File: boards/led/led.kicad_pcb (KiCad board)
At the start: 2 copper layers, 20 x 20 mm, 2 parts, among them J1 RJ45

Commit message: led pcb
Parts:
- moved J1 3.24 mm to (176.5, 104.1)
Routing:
- net Net-(D1-Pad2): track 0.00 -> 65.5 mm, vias 0 -> 1
- net Net-(D1-Pad1): track 0.00 -> 65.0 mm, vias 0 -> 1
- net Net-(D1-Pad3): track 0.00 -> 59.5 mm
- net Net-(D1-Pad4): track 0.00 -> 11.2 mm, vias 0 -> 1
- net Net-(D1-Pad5): track 0.00 -> 10.7 mm, vias 0 -> 1
- net Net-(D1-Pad6): track 0.00 -> 9.59 mm
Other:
- board size 20 x 20 mm -> 52.1 x 27.9 mm
- net class Default: clearance 0.4 -> 0.2; trace_width 0.25 -> 0.4
- rule trace_clearance: 0.4 -> 0.2
- board text added: "CUTOUT"
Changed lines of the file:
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@@
   (general
     (links 6)
-    (no_connects 6)
-    (area 0 0 0 0)
+    (no_connects 0)
+    (area 132.004999 90.094999 184.729001 118.185001)
     (thickness 1.6)
-    (drawings 4)
-    (tracks 0)
+    (drawings 9)
+    (tracks 38)
     (zones 0)
     (modules 2)
@@
   )
   (setup
-    (last_trace_width 0.25)
-    (trace_clearance 0.4)
+    (last_trace_width 0.4)
+    (trace_clearance 0.2)
     (zone_clearance 0.508)
     (zone_45_only yes)
@@
   (net 8 "Net-(J1-Pad8)")
   (net_class Default "This is the default net class."
-    (clearance 0.4)
-    (trace_width 0.25)
+    (clearance 0.2)
+    (trace_width 0.4)
     (via_dia 0.6)
     (via_drill 0.4)
@@
   )
   (module Connect:RJ45_8 (layer F.Cu)
-    (at 179.705 103.505 90)
+    (at 176.53 104.14 90)
     (tags RJ45)
     (fp_text reference J1 (at 0.254 4.826 90) (layer F.SilkS)
@@
     )
   )
+  (gr_line (start 132.08 118.11) (end 184.15 118.11) (angle 90) (layer Edge.Cuts) (width 0.15))
+  (gr_line (start 132.08 90.17) (end 132.08 118.11) (angle 90) (layer Edge.Cuts) (width 0.15))
+  (gr_line (start 184.15 90.17) (end 132.08 90.17) (angle 90) (layer Edge.Cuts) (width 0.15))
+  (gr_line (start 184.15 118.11) (end 184.15 90.17) (angle 90) (layer Edge.Cuts) (width 0.15))
+  (gr_text CUTOUT (at 149.225 104.775) (layer F.SilkS)
+    (effects (font (size 1.5 1.5) (thickness 0.3)))
+  )
   (gr_line (start 139 115) (end 139 95) (angle 90) (layer Edge.Cuts) (width 0.15))
   (gr_line (start 159 115) (end 139 115) (angle 90) (layer Edge.Cuts) (width 0.15))
   (gr_line (start 159 95) (end 159 115) (angle 90) (layer Edge.Cuts) (width 0.15))
   (gr_line (start 139 95) (end 159 95) (angle 90) (layer Edge.Cuts) (width 0.15))
+  (segment (start 170.18 106.045) (end 170.815 106.045) (width 0.25) (layer F.Cu) (net 1) (status 30))
+  (segment (start 170.815 106.045) (end 172.72 106.68) (width 0.4) (layer F.Cu) (net 1) (status 10))
+  (segment (start 172.72 106.68) (end 172.72 116.84) (width 0.4) (layer F.Cu) (net 1))
+  (segment (start 172.72 116.84) (end 134.62 116.84) (width 0.4) (layer F.Cu) (net 1))
+  (via (at 134.62 116.84) (size 0.6) (drill 0.4) (layers F.Cu B.Cu) (net 1))
+  (segment (start 134.62 116.84) (end 134.62 105.41) (width 0.4) (layer B.Cu) (net 1))
+  (segment (start 134.62 105.41) (end 135.03 105) (width 0.4) (layer B.Cu) (net 1))
+  (segment (start 135.03 105) (end 137.57 105) (width 0.4) (layer B.Cu) (net 1))
+  (segment (start 170.18 103.505) (end 170.815 103.505) (width 0.25) (layer B.Cu) (net 2) (status 30))
+  (segment (start 170.815 103.505) (end 172.72 104.14) (width 0.4) (layer B.Cu) (net 2) (status 10))
+  (segment (start 172.72 104.14) (end 172.72 116.84) (width 0.4) (layer B.Cu) (net 2))
+  (segment (start 172.72 116.84) (end 138.43 116.84) (width 0.4) (layer B.Cu) (net 2))
+  (segment (start 138.43 116.84) (end 137.57 116.43) (width 0.4) (layer B.Cu) (net 2))
+  (segment (start 137.57 116.43) (end 137.57 107.54) (width 0.4) (layer B.Cu) (net 2))
+  (segment (start 137.57 99.47) (end 137.57 102.46) (width 0.4) (layer B.Cu) (net 3))
+  (segment (start 137.16 99.06) (end 137.57 99.47) (width 0.4) (layer B.Cu) (net 3))
+  (via (at 137.16 99.06) (size 0.6) (drill 0.4) (layers F.Cu B.Cu) (net 3))
+  (segment (start 133.35 99.06) (end 137.16 99.06) (width 0.4) (layer F.Cu) (net 3))
+  (segment (start 133.35 102.87) (end 133.35 99.06) (width 0.4) (layer F.Cu) (net 3))
+  (segment (start 170.18 109.22) (end 166.37 115.57) (width 0.4) (layer F.Cu) (net 3) (status 10))
+  (segment (start 166.37 115.57) (end 133.35 115.57) (width 0.4) (layer F.Cu) (net 3))
+  (segment (start 133.35 115.57) (end 133.35 102.87) (width 0.4) (layer F.Cu) (net 3))
+  (segment (start 170.18 108.585) (end 170.18 109.22) (width 0.25) (layer F.Cu) (net 3) (status 30))
+  (segment (start 167.64 107.315) (end 167.64 106.68) (width 0.25) (layer B.Cu) (net 4) (status 10))
+  (segment (start 163.83 102.87) (end 160.84 102.87) (width 0.4) (layer B.Cu) (net 4))
+  (segment (start 167.64 106.68) (end 163.83 102.87) (width 0.4) (layer B.Cu) (net 4))
+  (segment (start 160.84 102.87) (end 160.43 102.46) (width 0.25) (layer B.Cu) (net 4))
+  (segment (start 167.64 104.775) (end 167.005 104.775) (width 0.25) (layer F.Cu) (net 5) (status 30))
+  (segment (start 167.005 104.775) (end 165.1 107.95) (width 0.4) (layer F.Cu) (net 5) (status 10))
+  (via (at 165.1 107.95) (size 0.6) (drill 0.4) (layers F.Cu B.Cu) (net 5))
+  (segment (start 165.1 107.95) (end 163.42 105) (width 0.4) (layer B.Cu) (net 5))
+  (segment (start 163.42 105) (end 160.43 105) (width 0.4) (layer B.Cu) (net 5))
+  (segment (start 167.64 102.235) (end 167.005 102.235) (width 0.25) (layer F.Cu) (net 6) (status 30))
+  (segment (start 167.005 102.235) (end 163.83 107.95) (width 0.4) (layer F.Cu) (net 6) (status 10))
+  (segment (start 163.42 107.54) (end 160.43 107.54) (width 0.4) (layer B.Cu) (net 6))
+  (segment (start 163.83 107.95) (end 163.42 107.54) (width 0.4) (layer B.Cu) (net 6))
+  (via (at 163.83 107.95) (size 0.6) (drill 0.4) (layers F.Cu B.Cu) (net 6))
+  (segment (start 160.88 107.54) (end 160.43 107.54) (width 0.25) (layer B.Cu) (net 6))
   (zone (net 0) (net_name "") (layer F.Cu) (hatch edge 0.508)
     (connect_pads (clearance 0.508))

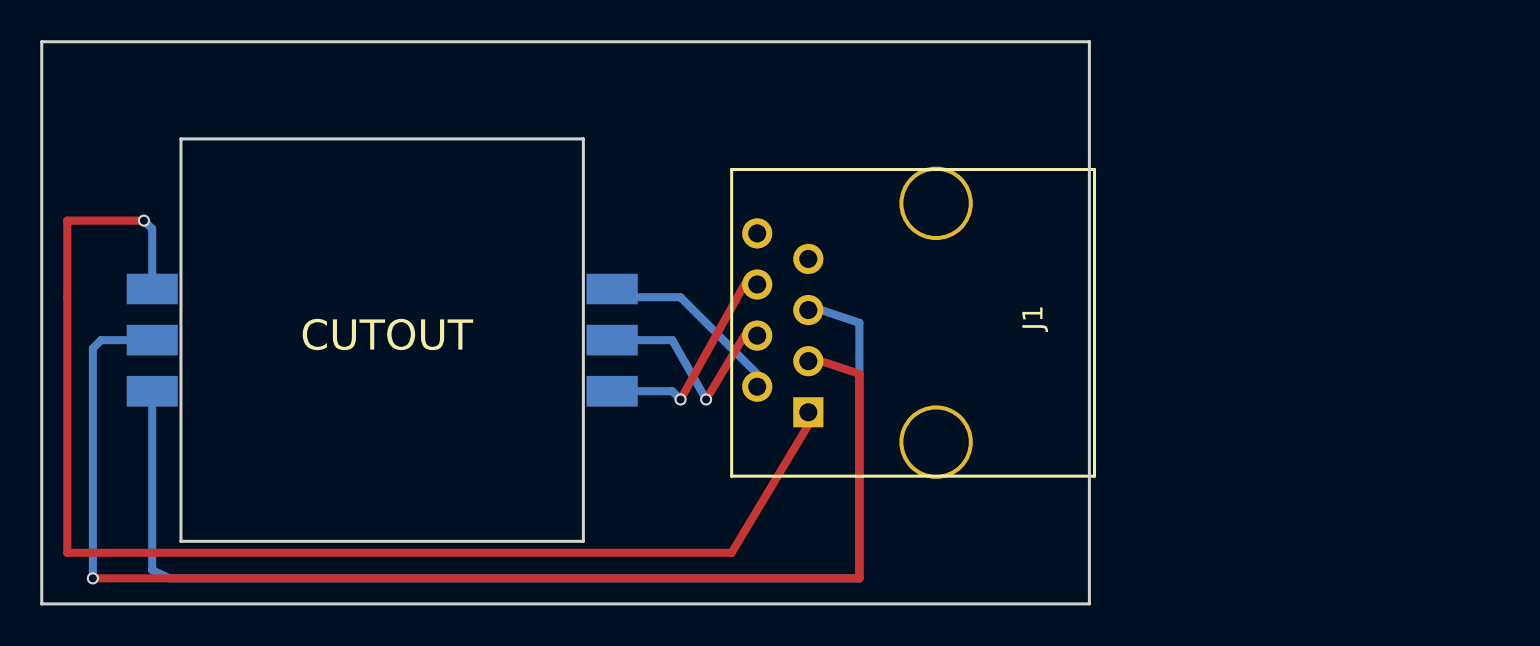
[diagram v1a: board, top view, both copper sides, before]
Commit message: added zones
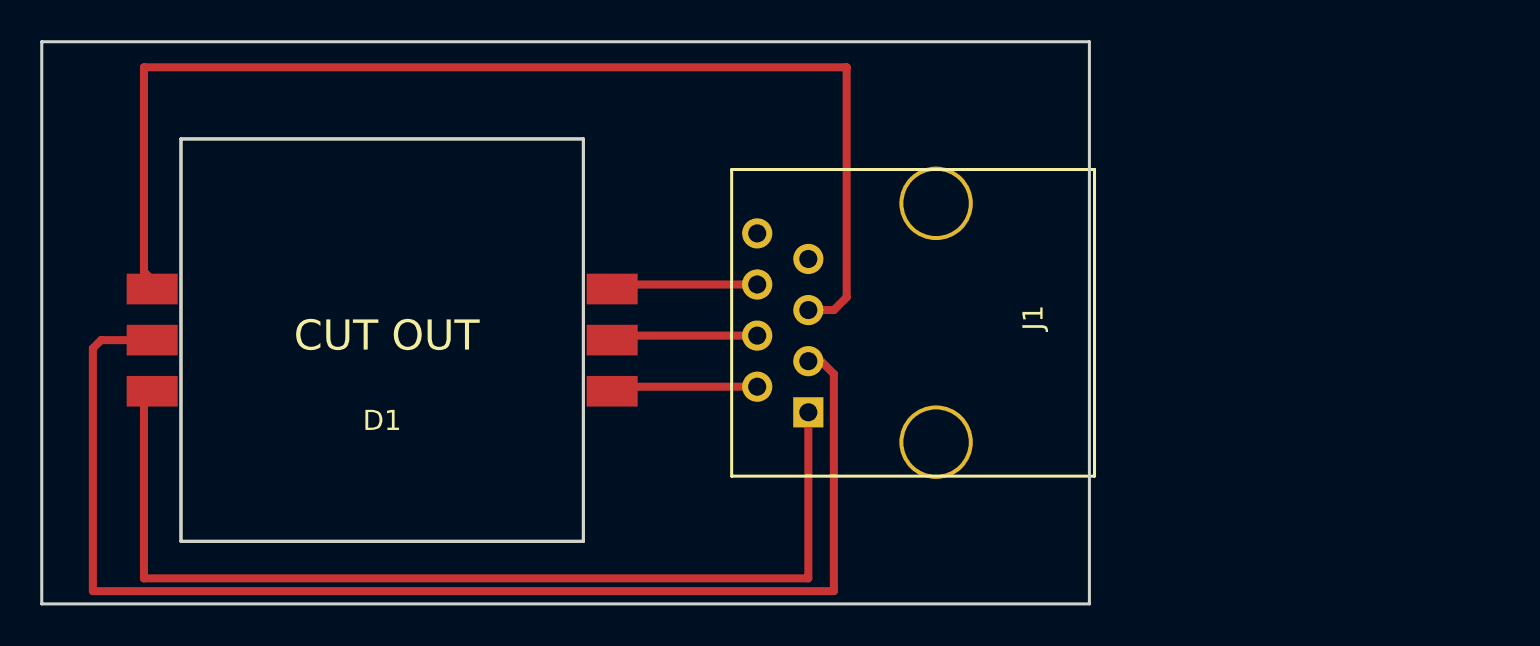
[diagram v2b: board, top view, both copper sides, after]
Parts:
- D1: moved to F.Cu
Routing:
- net Net-(D1-Pad1): track 65.0 -> 50.7 mm, vias 1 -> 0
- net Net-(D1-Pad4): track 11.2 -> 7.30 mm, vias 1 -> 0
- net Net-(D1-Pad5): track 10.7 -> 7.30 mm, vias 1 -> 0
- net Net-(D1-Pad6): track 9.59 -> 7.30 mm
- net Net-(D1-Pad2): track 65.5 -> 64.3 mm, vias 1 -> 0
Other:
- board text added: "CUT OUT"
- board text removed: "CUTOUT"
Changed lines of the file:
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@@
     (links 6)
     (no_connects 0)
-    (area 132.004999 90.094999 184.729001 118.185001)
+    (area 132.004999 90.094999 184.679001 118.185001)
     (thickness 1.6)
     (drawings 9)
-    (tracks 38)
+    (tracks 24)
     (zones 0)
     (modules 2)
@@
     (add_net "Net-(J1-Pad8)")
   )
-  (module lighting:10wled (layer B.Cu)
+  (module lighting:10wled (layer F.Cu)
     (at 149 105)
-    (fp_text reference D1 (at 0 -4) (layer B.SilkS)
-      (effects (font (size 1 1) (thickness 0.15)) (justify mirror))
-    )
-    (fp_text value LED_RGB (at 0 4) (layer B.Fab)
-      (effects (font (size 1 1) (thickness 0.15)) (justify mirror))
-    )
-    (fp_line (start -10 10) (end 10 10) (layer B.SilkS) (width 0.15))
-    (fp_line (start 10 10) (end 10 -10) (layer B.SilkS) (width 0.15))
-    (fp_line (start 10 -10) (end -10 -10) (layer B.SilkS) (width 0.15))
-    (fp_line (start -10 -10) (end -10 10) (layer B.SilkS) (width 0.15))
-    (pad 2 smd rect (at -11.43 0) (size 2.54 1.524) (layers B.Cu B.Paste B.Mask)
+    (fp_text reference D1 (at 0 4) (layer F.SilkS)
+      (effects (font (size 1 1) (thickness 0.15)))
+    )
+    (fp_text value LED_RGB (at 0 -4) (layer F.Fab)
+      (effects (font (size 1 1) (thickness 0.15)))
+    )
+    (fp_line (start -10 -10) (end 10 -10) (layer F.SilkS) (width 0.15))
+    (fp_line (start 10 -10) (end 10 10) (layer F.SilkS) (width 0.15))
+    (fp_line (start 10 10) (end -10 10) (layer F.SilkS) (width 0.15))
+    (fp_line (start -10 10) (end -10 -10) (layer F.SilkS) (width 0.15))
+    (pad 2 smd rect (at -11.43 0) (size 2.54 1.524) (layers F.Cu F.Paste F.Mask)
       (net 1 "Net-(D1-Pad2)"))
-    (pad 3 smd rect (at -11.43 2.54) (size 2.54 1.524) (layers B.Cu B.Paste B.Mask)
+    (pad 3 smd rect (at -11.43 -2.54) (size 2.54 1.524) (layers F.Cu F.Paste F.Mask)
       (net 2 "Net-(D1-Pad3)"))
-    (pad 1 smd rect (at -11.43 -2.54) (size 2.54 1.524) (layers B.Cu B.Paste B.Mask)
+    (pad 1 smd rect (at -11.43 2.54) (size 2.54 1.524) (layers F.Cu F.Paste F.Mask)
       (net 3 "Net-(D1-Pad1)"))
-    (pad 6 smd rect (at 11.43 -2.54) (size 2.54 1.524) (layers B.Cu B.Paste B.Mask)
+    (pad 6 smd rect (at 11.43 2.54) (size 2.54 1.524) (layers F.Cu F.Paste F.Mask)
       (net 4 "Net-(D1-Pad6)"))
-    (pad 5 smd rect (at 11.43 0) (size 2.54 1.524) (layers B.Cu B.Paste B.Mask)
+    (pad 5 smd rect (at 11.43 0) (size 2.54 1.524) (layers F.Cu F.Paste F.Mask)
       (net 5 "Net-(D1-Pad5)"))
-    (pad 4 smd rect (at 11.43 2.54) (size 2.54 1.524) (layers B.Cu B.Paste B.Mask)
+    (pad 4 smd rect (at 11.43 -2.54) (size 2.54 1.524) (layers F.Cu F.Paste F.Mask)
       (net 6 "Net-(D1-Pad4)"))
   )
@@
   (gr_line (start 184.15 90.17) (end 132.08 90.17) (angle 90) (layer Edge.Cuts) (width 0.15))
   (gr_line (start 184.15 118.11) (end 184.15 90.17) (angle 90) (layer Edge.Cuts) (width 0.15))
-  (gr_text CUTOUT (at 149.225 104.775) (layer F.SilkS)
+  (gr_text "CUT OUT" (at 149.225 104.775) (layer F.SilkS)
     (effects (font (size 1.5 1.5) (thickness 0.3)))
   )
@@
   (gr_line (start 159 95) (end 159 115) (angle 90) (layer Edge.Cuts) (width 0.15))
   (gr_line (start 139 95) (end 159 95) (angle 90) (layer Edge.Cuts) (width 0.15))
-  (segment (start 170.18 106.045) (end 170.815 106.045) (width 0.25) (layer F.Cu) (net 1) (status 30))
-  (segment (start 170.815 106.045) (end 172.72 106.68) (width 0.4) (layer F.Cu) (net 1) (status 10))
-  (segment (start 172.72 106.68) (end 172.72 116.84) (width 0.4) (layer F.Cu) (net 1))
-  (segment (start 172.72 116.84) (end 134.62 116.84) (width 0.4) (layer F.Cu) (net 1))
-  (via (at 134.62 116.84) (size 0.6) (drill 0.4) (layers F.Cu B.Cu) (net 1))
-  (segment (start 134.62 116.84) (end 134.62 105.41) (width 0.4) (layer B.Cu) (net 1))
-  (segment (start 134.62 105.41) (end 135.03 105) (width 0.4) (layer B.Cu) (net 1))
-  (segment (start 135.03 105) (end 137.57 105) (width 0.4) (layer B.Cu) (net 1))
-  (segment (start 170.18 103.505) (end 170.815 103.505) (width 0.25) (layer B.Cu) (net 2) (status 30))
-  (segment (start 170.815 103.505) (end 172.72 104.14) (width 0.4) (layer B.Cu) (net 2) (status 10))
-  (segment (start 172.72 104.14) (end 172.72 116.84) (width 0.4) (layer B.Cu) (net 2))
-  (segment (start 172.72 116.84) (end 138.43 116.84) (width 0.4) (layer B.Cu) (net 2))
-  (segment (start 138.43 116.84) (end 137.57 116.43) (width 0.4) (layer B.Cu) (net 2))
-  (segment (start 137.57 116.43) (end 137.57 107.54) (width 0.4) (layer B.Cu) (net 2))
-  (segment (start 137.57 99.47) (end 137.57 102.46) (width 0.4) (layer B.Cu) (net 3))
-  (segment (start 137.16 99.06) (end 137.57 99.47) (width 0.4) (layer B.Cu) (net 3))
-  (via (at 137.16 99.06) (size 0.6) (drill 0.4) (layers F.Cu B.Cu) (net 3))
-  (segment (start 133.35 99.06) (end 137.16 99.06) (width 0.4) (layer F.Cu) (net 3))
-  (segment (start 133.35 102.87) (end 133.35 99.06) (width 0.4) (layer F.Cu) (net 3))
-  (segment (start 170.18 109.22) (end 166.37 115.57) (width 0.4) (layer F.Cu) (net 3) (status 10))
-  (segment (start 166.37 115.57) (end 133.35 115.57) (width 0.4) (layer F.Cu) (net 3))
-  (segment (start 133.35 115.57) (end 133.35 102.87) (width 0.4) (layer F.Cu) (net 3))
-  (segment (start 170.18 108.585) (end 170.18 109.22) (width 0.25) (layer F.Cu) (net 3) (status 30))
-  (segment (start 167.64 107.315) (end 167.64 106.68) (width 0.25) (layer B.Cu) (net 4) (status 10))
-  (segment (start 163.83 102.87) (end 160.84 102.87) (width 0.4) (layer B.Cu) (net 4))
-  (segment (start 167.64 106.68) (end 163.83 102.87) (width 0.4) (layer B.Cu) (net 4))
-  (segment (start 160.84 102.87) (end 160.43 102.46) (width 0.25) (layer B.Cu) (net 4))
-  (segment (start 167.64 104.775) (end 167.005 104.775) (width 0.25) (layer F.Cu) (net 5) (status 30))
-  (segment (start 167.005 104.775) (end 165.1 107.95) (width 0.4) (layer F.Cu) (net 5) (status 10))
-  (via (at 165.1 107.95) (size 0.6) (drill 0.4) (layers F.Cu B.Cu) (net 5))
-  (segment (start 165.1 107.95) (end 163.42 105) (width 0.4) (layer B.Cu) (net 5))
-  (segment (start 163.42 105) (end 160.43 105) (width 0.4) (layer B.Cu) (net 5))
-  (segment (start 167.64 102.235) (end 167.005 102.235) (width 0.25) (layer F.Cu) (net 6) (status 30))
-  (segment (start 167.005 102.235) (end 163.83 107.95) (width 0.4) (layer F.Cu) (net 6) (status 10))
-  (segment (start 163.42 107.54) (end 160.43 107.54) (width 0.4) (layer B.Cu) (net 6))
-  (segment (start 163.83 107.95) (end 163.42 107.54) (width 0.4) (layer B.Cu) (net 6))
-  (via (at 163.83 107.95) (size 0.6) (drill 0.4) (layers F.Cu B.Cu) (net 6))
-  (segment (start 160.88 107.54) (end 160.43 107.54) (width 0.25) (layer B.Cu) (net 6))
+  (segment (start 170.18 106.045) (end 170.815 106.045) (width 0.4) (layer F.Cu) (net 1))
+  (segment (start 170.815 106.045) (end 171.45 106.68) (width 0.4) (layer F.Cu) (net 1))
+  (segment (start 171.45 106.68) (end 171.45 117.475) (width 0.4) (layer F.Cu) (net 1))
+  (segment (start 171.45 117.475) (end 134.62 117.475) (width 0.4) (layer F.Cu) (net 1))
+  (segment (start 134.62 117.475) (end 134.62 105.41) (width 0.4) (layer F.Cu) (net 1))
+  (segment (start 134.62 105.41) (end 135.03 105) (width 0.4) (layer F.Cu) (net 1))
+  (segment (start 135.03 105) (end 137.57 105) (width 0.4) (layer F.Cu) (net 1))
+  (segment (start 170.18 103.505) (end 171.45 103.505) (width 0.4) (layer F.Cu) (net 2) (status 400000))
+  (segment (start 137.16 101.6) (end 137.57 102.01) (width 0.4) (layer F.Cu) (net 2) (status 800000))
+  (segment (start 137.16 91.44) (end 137.16 101.6) (width 0.4) (layer F.Cu) (net 2))
+  (segment (start 172.085 91.44) (end 137.16 91.44) (width 0.4) (layer F.Cu) (net 2))
+  (segment (start 172.085 102.87) (end 172.085 91.44) (width 0.4) (layer F.Cu) (net 2))
+  (segment (start 171.45 103.505) (end 172.085 102.87) (width 0.4) (layer F.Cu) (net 2))
+  (segment (start 137.57 102.01) (end 137.57 102.46) (width 0.4) (layer F.Cu) (net 2) (status C00000))
+  (segment (start 170.18 108.585) (end 170.18 116.84) (width 0.4) (layer F.Cu) (net 3))
+  (segment (start 137.16 116.84) (end 137.16 107.95) (width 0.4) (layer F.Cu) (net 3))
+  (segment (start 170.18 116.84) (end 137.16 116.84) (width 0.4) (layer F.Cu) (net 3))
+  (segment (start 137.16 107.95) (end 137.57 107.54) (width 0.4) (layer F.Cu) (net 3))
+  (segment (start 167.64 107.315) (end 160.655 107.315) (width 0.4) (layer F.Cu) (net 4))
+  (segment (start 160.655 107.315) (end 160.43 107.54) (width 0.4) (layer F.Cu) (net 4))
+  (segment (start 167.64 104.775) (end 160.655 104.775) (width 0.4) (layer F.Cu) (net 5))
+  (segment (start 160.655 104.775) (end 160.43 105) (width 0.4) (layer F.Cu) (net 5))
+  (segment (start 167.64 102.235) (end 160.655 102.235) (width 0.4) (layer F.Cu) (net 6))
+  (segment (start 160.655 102.235) (end 160.43 102.46) (width 0.4) (layer F.Cu) (net 6))
   (zone (net 0) (net_name "") (layer F.Cu) (hatch edge 0.508)
     (connect_pads (clearance 0.508))

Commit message: another revision
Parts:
- added P1: CONN_01X08, Pin_Headers:Pin_Header_Straight_1x08, F.Cu at (184.8, 92.7)
- added REF**: MountingHole_2-5mm, Mounting_Holes:MountingHole_2-5mm, F.Cu at (169.5, 111.8)
- added REF**: MountingHole_2-5mm, Mounting_Holes:MountingHole_2-5mm, F.Cu at (169.5, 96.5)
- moved J1 18.4 mm to (194.9, 104.1)
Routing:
- net Net-(D1-Pad4): track 7.30 -> 47.3 mm
- net Net-(D1-Pad5): track 7.30 -> 47.1 mm
- net Net-(D1-Pad6): track 7.30 -> 44.5 mm
- net Net-(D1-Pad1): track 50.7 -> 84.1 mm
- net Net-(D1-Pad2): track 64.3 -> 96.5 mm
- net Net-(J1-Pad7): track 0.00 -> 24.5 mm
- net Net-(D1-Pad3): track 59.7 -> 82.4 mm
- net Net-(J1-Pad8): track 0.00 -> 19.8 mm
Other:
- board size 52.1 x 27.9 mm -> 72.4 x 27.9 mm
